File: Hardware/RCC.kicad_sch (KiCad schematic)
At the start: 5 parts, among them J1 Battery

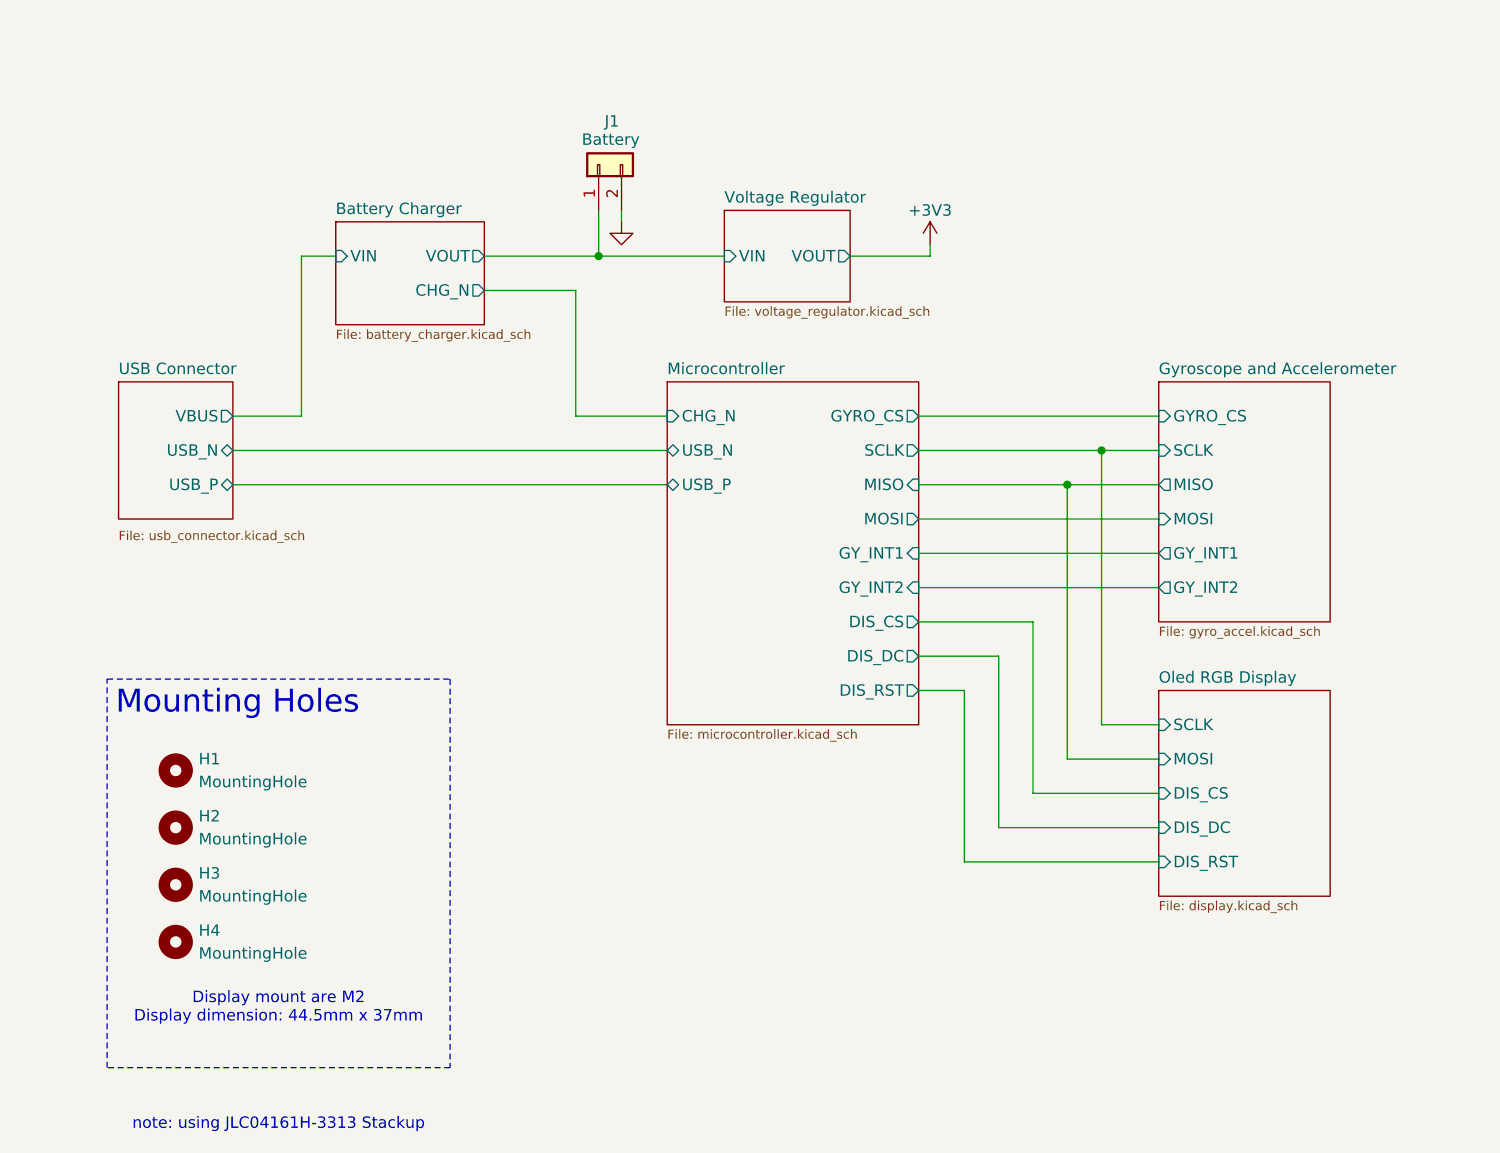
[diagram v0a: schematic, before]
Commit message: Restructure folders
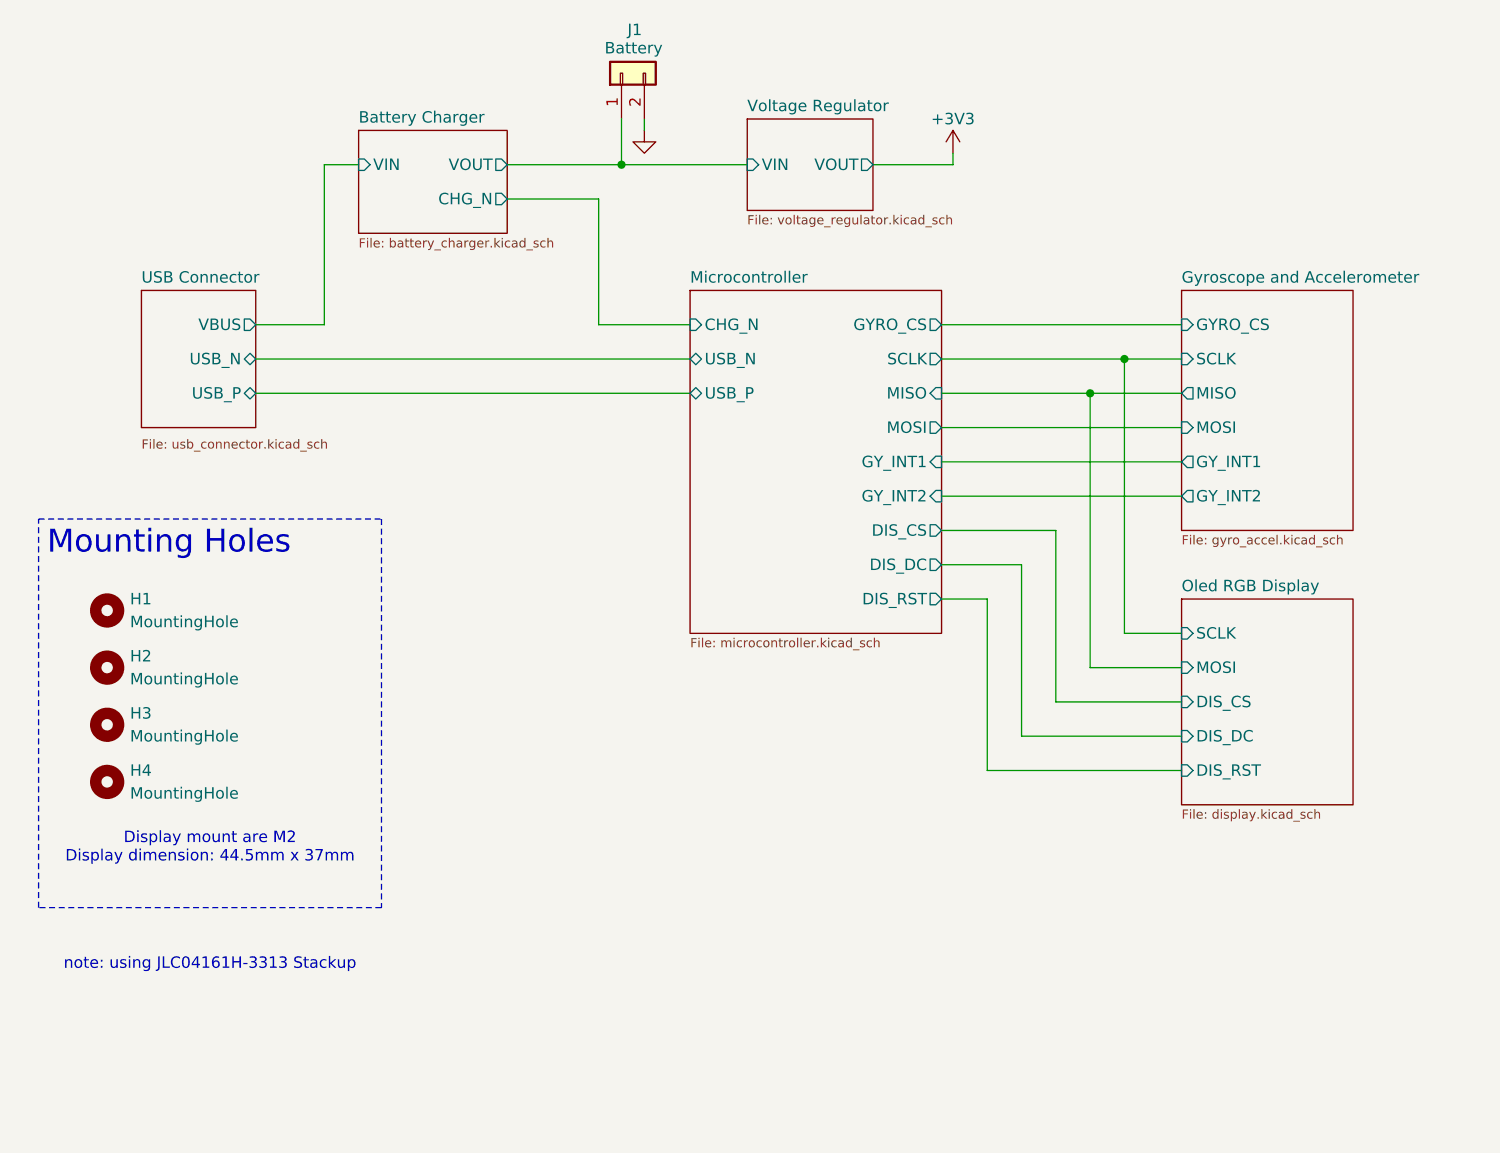
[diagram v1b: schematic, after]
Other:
- title: Robot Companion -> Robot Car Companion (DashiDaaa)
- moved on the sheet: H1, H2, H3, H4, J1
